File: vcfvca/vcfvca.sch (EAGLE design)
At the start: 63 parts, among them IC1 LM13700N, IC2 LM4558N, IC3 LM13700N, IC4 LM13700N, Q1 BF245, Q2 BF245, Q3 2N3906, Q4 BF245, Q5 BF245, Q6 2N3906

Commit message: Add VCF freq and res control current generator
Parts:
- added IC5: LM4558N, linear:LM4558N
- added Q7, Q9: 2N3906, transistor-small-signal:2N3906
- added Q8: 2N3904, transistor-small-signal:2N3904
- added R39: 49k9, rcl:R-US_0207/10
- added R40: 1k TC, rcl:R-US_0207/10
- added R41, R42: 100k 1%, rcl:R-US_0207/10
- added R43: 18k, rcl:R-US_0207/10
- added R44: 47k, rcl:R-US_0207/10
- added R45: 100k, rcl:R-US_0207/10
- added R46: 4k7, rcl:R-US_0207/10
- added VR3, VR4: 10k, pot:TRIM_US-S63P
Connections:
- new net N$38: IC5A.OUT, R42.2, VR3.A
- new net N$39: R39.1, VR3.E, VR3.S
- new net N$40: Q8.B, R39.2, R40.1
- new net N$41: IC5A.+IN, R43.1
- new net N$42: IC5A.-IN, R42.1
- new net N$43: Q7.B, Q8.E, R41.1
- new net N$44: R46.2, VR4.E, VR4.S
- new net N$46: Q9.E, R45.2, R46.1
- new net N$47: IC5B.OUT, Q9.B
- new net N$48: IC5B.-IN, R44.2, R45.1
- net -15V: now also R41.2
- net GND: now also IC5B.+IN, Q7.E, Q8.C, R40.2, R43.2, VR4.A
- net I_FREQ: now also Q7.C
- net I_RES: now also Q9.C
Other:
- note added: "R41 R42 matched"
- moved on the sheet: C1, C2, IC1P, IC3P, IC4P, J1

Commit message: Finished drawing the schematics. Adapted RES current source for AMP.
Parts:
- added C12, C13, C14, C15, C16, C17, C18, C19, C20, C21: 100n, rcl:C-EU050-025X075
- added J2: FREQ, pinhead:PINHD-1X2
- added J3: RES, pinhead:PINHD-1X2
- added J4: AMP, pinhead:PINHD-1X2
- added J5: AUD_IN, pinhead:PINHD-1X2
- added J6: AUD_OUT, pinhead:PINHD-1X2
- added Q10: 2N3906, transistor-small-signal:2N3906
- added R47: 100k 1%, rcl:R-US_0207/10
- added R48: 301k 1%, rcl:R-US_0207/10
- added R49: 47k, rcl:R-US_0207/10
- added R50: 22k, rcl:R-US_0207/10
- added R51: 4k7, rcl:R-US_0207/10
- added R52, R53: 150k, rcl:R-US_0207/10
- added VR5: 10k, pot:TRIM_US-S63P
- added VR6, VR7: 100k, pot:TRIM_US-B64Y
- added VR8: (no value), pot:TRIM_US-B64Y
- J1: value (none) -> POWER
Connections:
- new net N$45: R51.2, VR5.E, VR5.S
- new net N$49: Q10.E, R50.2, R51.1
- new net N$50: IC2B.OUT, Q10.B
- new net N$51: J2.1, R47.1
- new net N$52: IC2B.-IN, R49.2, R50.1, R53.2
- new net N$53: J4.1, R49.1
- new net N$54: R48.1, VR6.S
- new net N$55: J5.1, R1.1
- new net N$56: J3.1, R44.1
- new net N$57: C10.-, J6.1
- new net N$58: R52.1, VR7.S
- new net N$60: R53.1, VR8.S
- net +15V: now also C12.1, C14.1, C16.1, C18.1, C20.1, IC1P.V+, IC2P.V+, IC3P.V+, IC4P.V+, IC5P.V+, VR6.E, VR7.E, VR8.E
- net -15V: now also C13.2, C15.2, C17.2, C19.2, C21.2, IC1P.V-, IC2P.V-, IC3P.V-, IC4P.V-, IC5P.V-
- net GND: now also C12.2, C13.1, C14.2, C15.1, C16.2, C17.1, C18.2, C19.1, C20.2, C21.1, IC2B.+IN, J2.2, J3.2, J4.2, J5.2, J6.2, VR5.A, VR6.A, VR7.A, VR8.A
- net I_AMP: now also Q10.C
- net N$42: now also R47.2, R48.2
- net N$48: now also R52.2
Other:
- note added: "4-pole VCF"
- note added: "CV 0~5 volts"
- note added: "Resonance feedback"
- note added: "VCA"
- note added: "VR4 at middle Full-scale: 1.086 mA"
- note added: "VR5 at middle Full-scale: 269 uA"
- moved on the sheet: C1, C10, C11, C2, C3, C4, C5, C6, C7, C8, C9, IC1A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

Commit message: Run and approve ERC
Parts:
- VR8: value (none) -> 100k
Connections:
- removed net N$1: C1.+
- net +15V: now also C1.+
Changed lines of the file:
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@@
 <part name="VR6" library="pot" library_urn="urn:adsk.eagle:library:331" deviceset="TRIM_US-" device="B64Y" package3d_urn="urn:adsk.eagle:package:22690/1" value="100k"/>
 <part name="VR7" library="pot" library_urn="urn:adsk.eagle:library:331" deviceset="TRIM_US-" device="B64Y" package3d_urn="urn:adsk.eagle:package:22690/1" value="100k"/>
-<part name="VR8" library="pot" library_urn="urn:adsk.eagle:library:331" deviceset="TRIM_US-" device="B64Y" package3d_urn="urn:adsk.eagle:package:22690/1"/>
+<part name="VR8" library="pot" library_urn="urn:adsk.eagle:library:331" deviceset="TRIM_US-" device="B64Y" package3d_urn="urn:adsk.eagle:package:22690/1" value="100k"/>
 <part name="J2" library="pinhead" library_urn="urn:adsk.eagle:library:325" deviceset="PINHD-1X2" device="" package3d_urn="urn:adsk.eagle:package:22435/2" value="FREQ"/>
 <part name="J3" library="pinhead" library_urn="urn:adsk.eagle:library:325" deviceset="PINHD-1X2" device="" package3d_urn="urn:adsk.eagle:package:22435/2" value="RES"/>
@@
 <net name="+15V" class="0">
 <segment>
-<pinref part="J1" gate="G$3" pin="1"/>
-<wire x1="248.92" y1="241.3" x2="254" y2="241.3" width="0.1524" layer="91"/>
-<wire x1="254" y1="241.3" x2="254" y2="248.92" width="0.1524" layer="91"/>
 <pinref part="SUPPLY1" gate="+15V" pin="+15V"/>
-<wire x1="254" y1="248.92" x2="271.78" y2="248.92" width="0.1524" layer="91"/>
 <pinref part="IC5" gate="P" pin="V+"/>
 <wire x1="271.78" y1="248.92" x2="279.4" y2="248.92" width="0.1524" layer="91"/>
@@
 <wire x1="353.06" y1="248.92" x2="360.68" y2="248.92" width="0.1524" layer="91"/>
 <wire x1="360.68" y1="248.92" x2="360.68" y2="243.84" width="0.1524" layer="91"/>
-<junction x="271.78" y="248.92"/>
 <pinref part="IC4" gate="P" pin="V+"/>
 <wire x1="353.06" y1="243.84" x2="353.06" y2="248.92" width="0.1524" layer="91"/>
@@
 <wire x1="279.4" y1="246.38" x2="279.4" y2="248.92" width="0.1524" layer="91"/>
 <junction x="279.4" y="248.92"/>
+<wire x1="254" y1="241.3" x2="254" y2="248.92" width="0.1524" layer="91"/>
+<pinref part="J1" gate="G$3" pin="1"/>
+<wire x1="248.92" y1="241.3" x2="254" y2="241.3" width="0.1524" layer="91"/>
+<pinref part="C1" gate="G$1" pin="+"/>
+<wire x1="264.16" y1="246.38" x2="264.16" y2="248.92" width="0.1524" layer="91"/>
+<wire x1="254" y1="248.92" x2="264.16" y2="248.92" width="0.1524" layer="91"/>
+<wire x1="264.16" y1="248.92" x2="271.78" y2="248.92" width="0.1524" layer="91"/>
+<junction x="264.16" y="248.92"/>
+<junction x="271.78" y="248.92"/>
 </segment>
 <segment>
@@
 <pinref part="GND29" gate="1" pin="GND"/>
 <wire x1="38.1" y1="40.64" x2="38.1" y2="38.1" width="0.1524" layer="91"/>
-<wire x1="27.94" y1="40.64" x2="30.48" y2="40.64" width="0.1524" layer="91"/>
 </segment>
 <segment>
@@
 <pinref part="GND35" gate="1" pin="GND"/>
 <wire x1="350.52" y1="177.8" x2="350.52" y2="175.26" width="0.1524" layer="91"/>
-</segment>
-</net>
-<net name="N$1" class="0">
-<segment>
-<junction x="264.16" y="248.92"/>
-<pinref part="C1" gate="G$1" pin="+"/>
-<wire x1="264.16" y1="246.38" x2="264.16" y2="248.92" width="0.1524" layer="91"/>
 </segment>
 </net>
@@
 <pinref part="J5" gate="G$1" pin="1"/>
 <pinref part="R1" gate="G$1" pin="1"/>
-<wire x1="7.62" y1="210.82" x2="10.16" y2="210.82" width="0.1524" layer="91"/>
-<wire x1="10.16" y1="210.82" x2="17.78" y2="210.82" width="0.1524" layer="91"/>
-<wire x1="17.78" y1="210.82" x2="20.32" y2="210.82" width="0.1524" layer="91"/>
+<wire x1="7.62" y1="210.82" x2="17.78" y2="210.82" width="0.1524" layer="91"/>
 </segment>
 </net>
@@
 </sheet>
 </sheets>
+<errors>
+</errors>
 </schematic>
 </drawing>

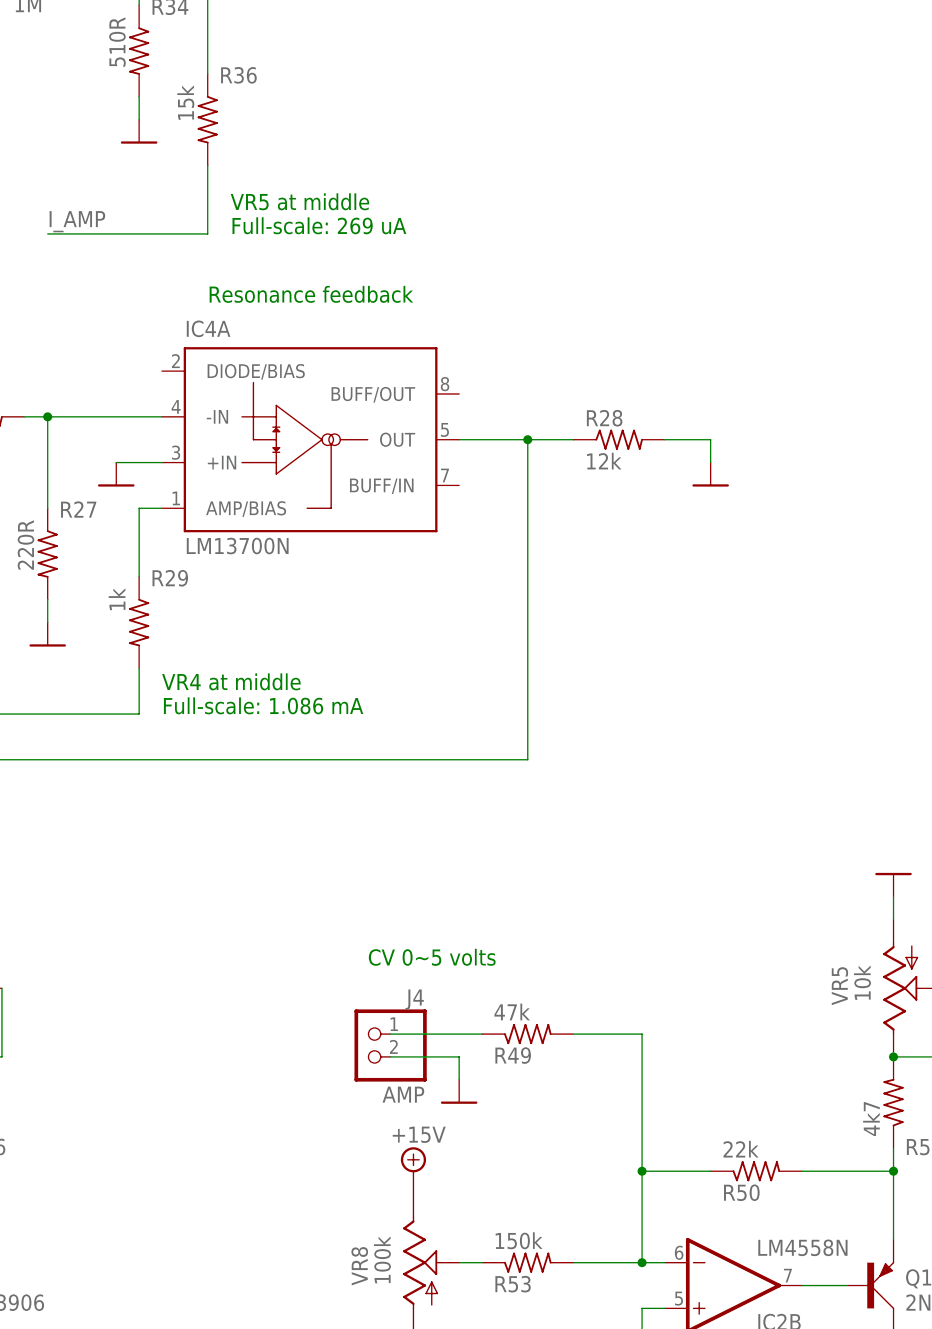
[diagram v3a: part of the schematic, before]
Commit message: Fix VCA scale and feedback resistor
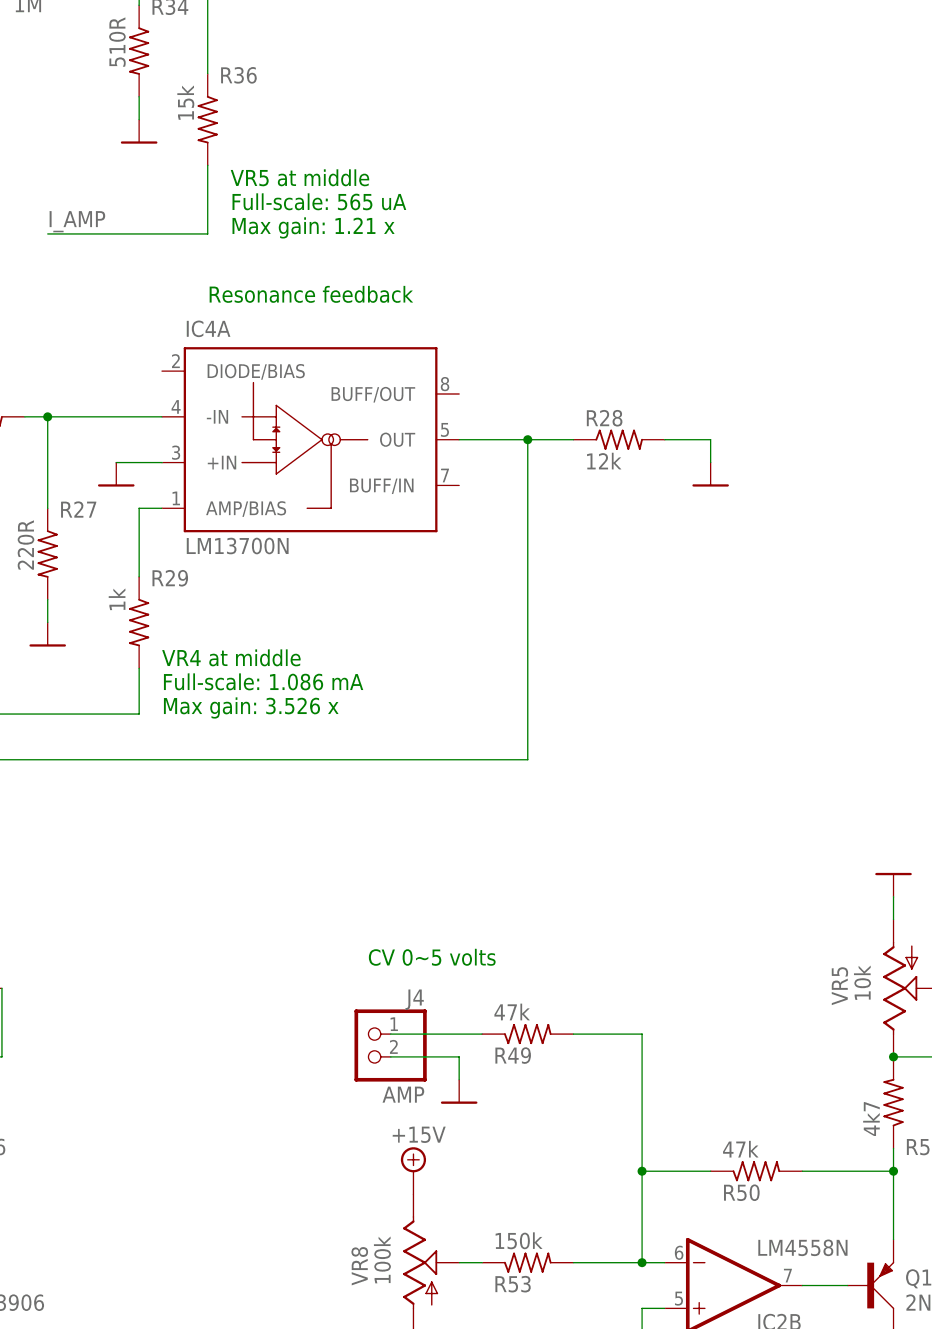
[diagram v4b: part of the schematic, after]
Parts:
- R50: value 22k -> 47k
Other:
- note added: "VR4 at middle Full-scale: 1.086 mA Max gain: 3.526 x"
- note added: "VR5 at middle Full-scale: 565 uA Max gain: 1.21 x"
- note removed: "VR4 at middle Full-scale: 1.086 mA"
- note removed: "VR5 at middle Full-scale: 269 uA"
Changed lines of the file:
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@@
 <part name="R48" library="rcl" library_urn="urn:adsk.eagle:library:334" deviceset="R-US_" device="0207/10" package3d_urn="urn:adsk.eagle:package:23491/2" value="301k 1%"/>
 <part name="R49" library="rcl" library_urn="urn:adsk.eagle:library:334" deviceset="R-US_" device="0207/10" package3d_urn="urn:adsk.eagle:package:23491/2" value="47k"/>
-<part name="R50" library="rcl" library_urn="urn:adsk.eagle:library:334" deviceset="R-US_" device="0207/10" package3d_urn="urn:adsk.eagle:package:23491/2" value="22k"/>
+<part name="R50" library="rcl" library_urn="urn:adsk.eagle:library:334" deviceset="R-US_" device="0207/10" package3d_urn="urn:adsk.eagle:package:23491/2" value="47k"/>
 <part name="R51" library="rcl" library_urn="urn:adsk.eagle:library:334" deviceset="R-US_" device="0207/10" package3d_urn="urn:adsk.eagle:package:23491/2" value="4k7"/>
 <part name="VR5" library="pot" library_urn="urn:adsk.eagle:library:331" deviceset="TRIM_US-" device="S63P" package3d_urn="urn:adsk.eagle:package:22705/1" value="10k"/>
@@
 <text x="284.48" y="50.8" size="1.778" layer="91">CV 0~5 volts</text>
 <text x="269.24" y="132.08" size="1.778" layer="91">VR5 at middle
-Full-scale: 269 uA</text>
+Full-scale: 565 uA
+Max gain: 1.21 x</text>
 <text x="261.62" y="78.74" size="1.778" layer="91">VR4 at middle
-Full-scale: 1.086 mA</text>
+Full-scale: 1.086 mA
+Max gain: 3.526 x</text>
 <text x="129.54" y="236.22" size="1.778" layer="91">4-pole VCF</text>
 <text x="284.48" y="198.12" size="1.778" layer="91">VCA</text>
